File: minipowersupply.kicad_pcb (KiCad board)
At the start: 2 copper layers, 110.2 x 85.7 mm, 128 parts, among them J1 Conn_01x01_Female, J10 Conn_01x08_Male, J2 Conn_01x01_Female, J3 Conn_01x01_Female, J4 Conn_01x01_Female, J5 Conn_01x01_Female, J6 Conn_01x01_Female, J7 Conn_01x01_Female, J8 Conn_01x02_Female, J9 Conn_01x02_Female, Q1 BC817, U1 LM317_TO-220, U10 74HC4051, U11 74HC4051, U12 LM358, U13 LM358, U2 LM337_TO220, U3 LM7805_TO220, U4 ACS70331EOLCTR-2P5U3, U5 ACS70331EOLCTR-2P5U3, U6 ACS70331EOLCTR-2P5U3, U7 ACS70331EOLCTR-2P5U3, U8 ACS70331EOLCTR-2P5U3, U9 LM358

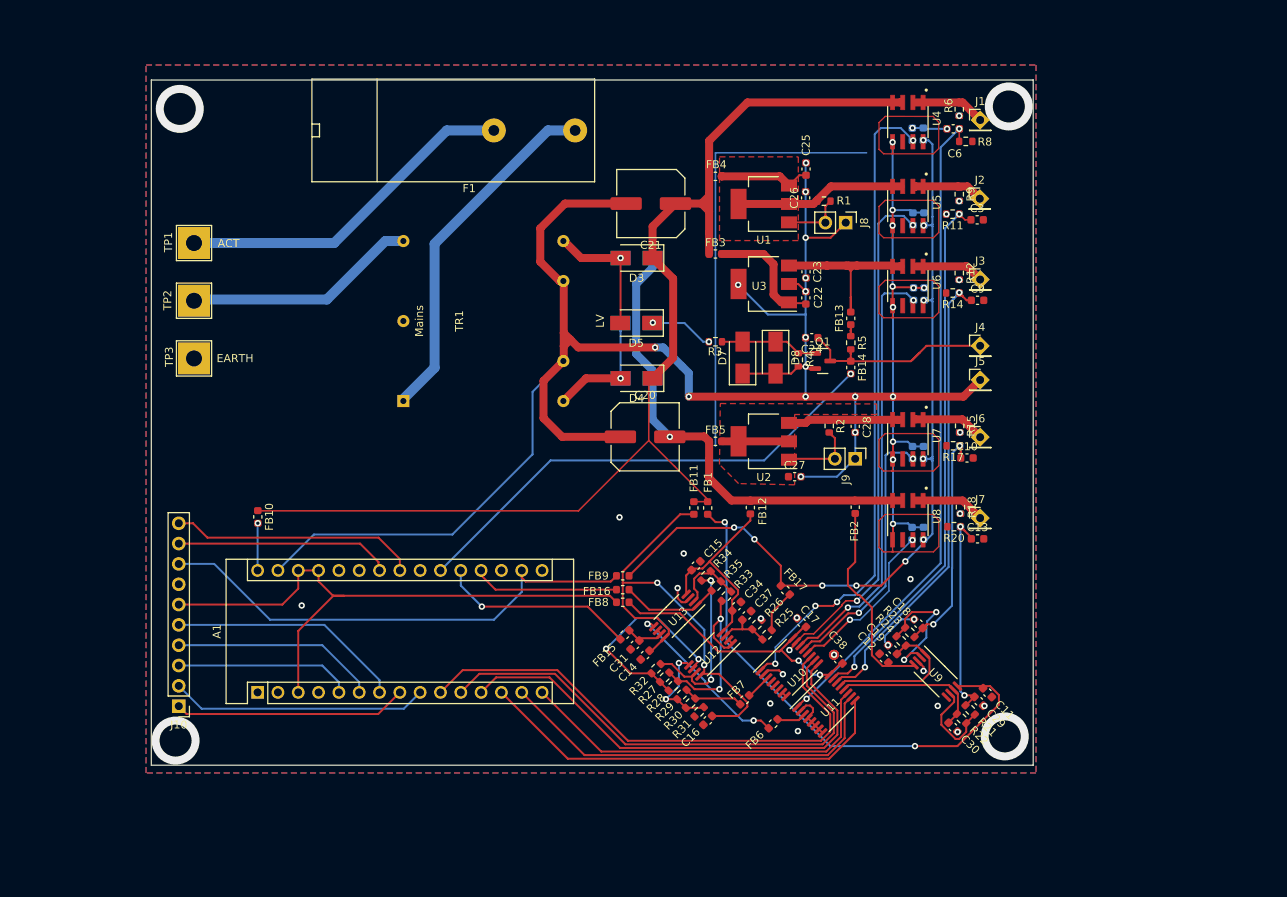
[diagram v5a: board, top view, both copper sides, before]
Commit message: updated with extra filtering and guard ring placement
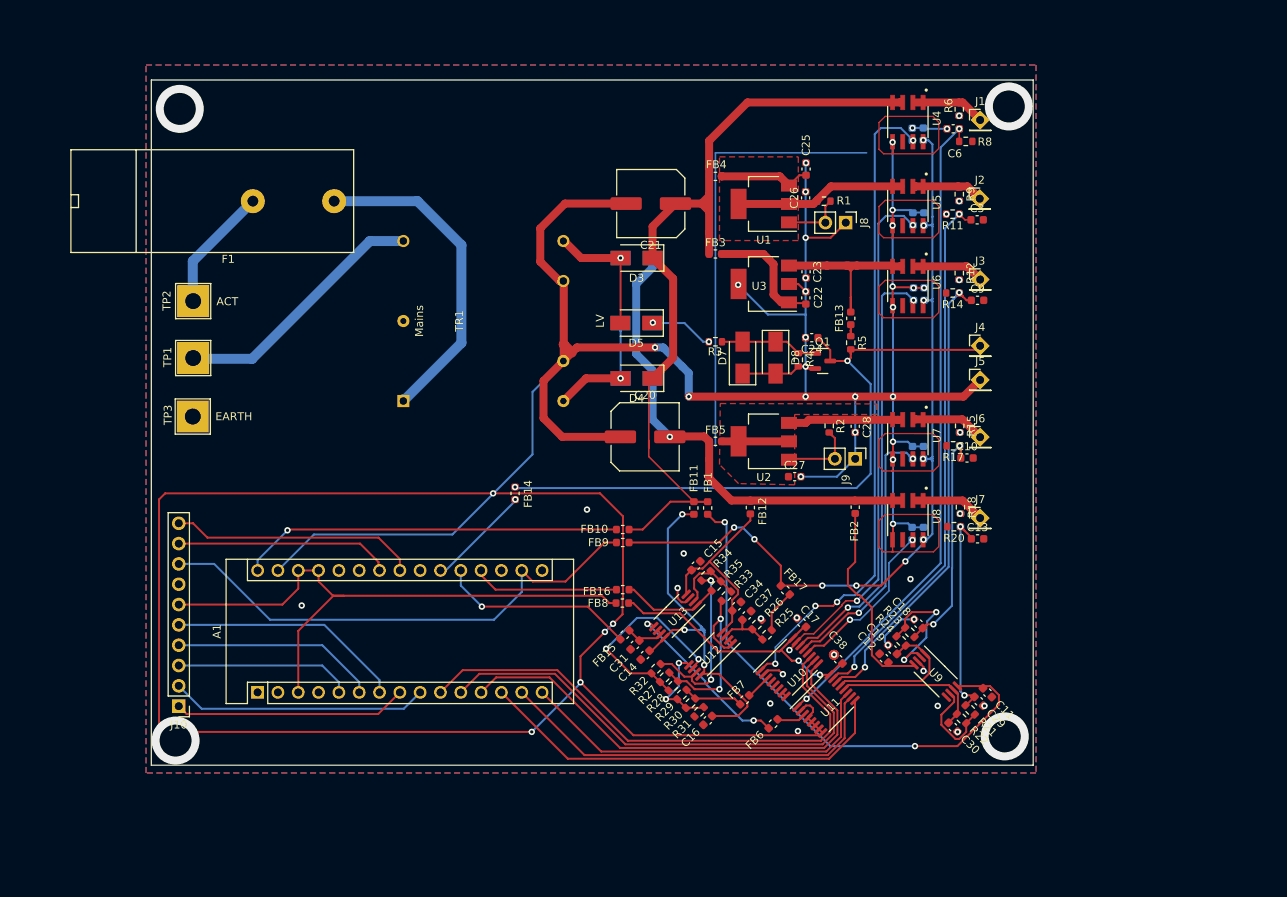
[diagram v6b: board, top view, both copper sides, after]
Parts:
- moved FB10 45.6 mm to (144.8, 105.3), turned to 180 degrees
- moved FB14 44.8 mm to (131.3, 100.8)
- moved F1 31.4 mm to (108.7, 64.3)
- moved TP1 14.4 mm to (91.1, 83.9)
- moved TP3 7.27 mm to (91.0, 91.2)
- moved FB9 4.17 mm to (144.8, 107.0)
- moved FB8 0.11 mm to (144.7, 114.5)
- moved TP2 0.11 mm to (91.1, 76.8)
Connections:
- TP1 pad 1: Net-(F1-Pad2) -> Net-(TR1-Pad2)
- TP2 pad 1: Net-(TP2-Pad1) -> Net-(F1-Pad2)
- TR1 pad 2: Net-(TP2-Pad1) -> Net-(TR1-Pad2)
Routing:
- net GNDREF: track 322.4 -> 523.0 mm, vias 49 -> 54
- net /Clock and TTL/Ck_Out: track 27.5 -> 86.8 mm, vias 0 -> 2
- net Net-(A1-Pad21): track 61.5 -> 12.9 mm
- net Net-(A1-Pad30): track 5.92 -> 47.7 mm
- net VUnreg+: track 148.1 -> 107.1 mm
- net Net-(TR1-Pad2): track 0.00 -> 32.4 mm
- net Net-(TP2-Pad1): track 29.6 -> 0.00 mm
- net Net-(F1-Pad2): track 43.5 -> 15.6 mm
- net Net-(C14-Pad1): track 58.5 -> 47.1 mm, vias 2 -> 3
- net Net-(F1-Pad1): track 45.0 -> 41.2 mm
- net 3V3: track 104.1 -> 102.4 mm
- net Net-(A1-Pad17): track 63.1 -> 64.3 mm
